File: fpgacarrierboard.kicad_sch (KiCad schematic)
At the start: 0 parts

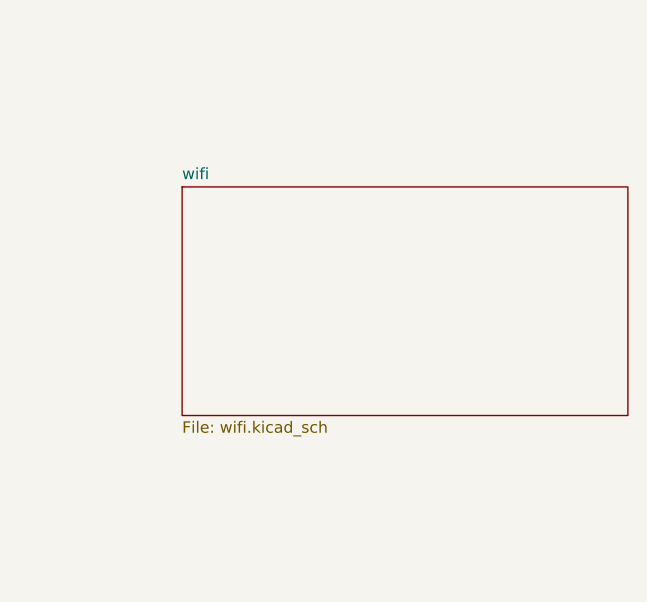
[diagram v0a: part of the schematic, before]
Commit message: Remove optional WiFi sheet from schematic and PCB
- Delete wifi sheet and its seven parts; restore no-connect flags on the five freed FPGA bank-34 pins
- Reduce J4 pad solder-mask margin so the fine-pitch pads meet the 0.1mm web rule
- Regenerate BOM and ERC report
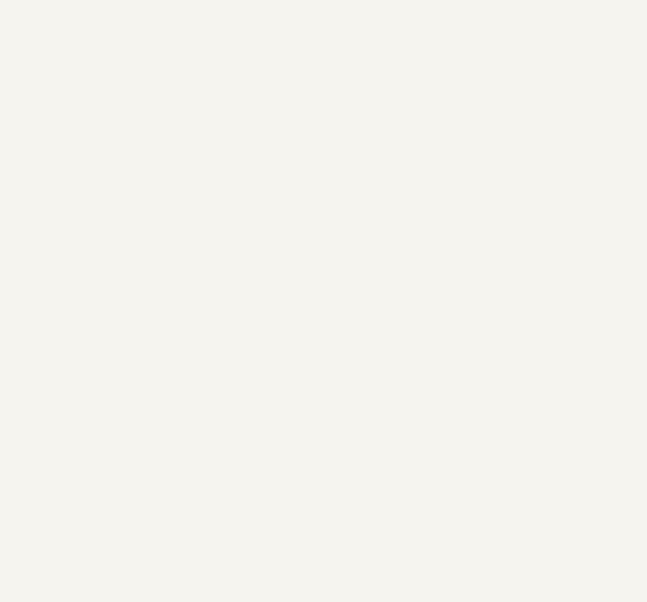
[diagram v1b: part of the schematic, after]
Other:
- removed sheet wifi
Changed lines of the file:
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@@
-	)
-	(sheet
-		(at 186.69 69.85)
-		(size 49.53 25.4)
-		(exclude_from_sim no)
-		(in_bom yes)
-		(on_board yes)
-		(dnp no)
-		(fields_autoplaced yes)
-		(stroke
-			(width 0.1524)
-			(type solid)
-		)
-		(fill
-			(color 0 0 0 0)
-		)
-		(property "Sheetname" "wifi"
-			(at 186.69 69.1384 0)
-			(show_name no)
-			(do_not_autoplace no)
-			(effects
-				(font
-					(size 1.27 1.27)
-				)
-				(justify left bottom)
-			)
-		)
-		(property "Sheetfile" "wifi.kicad_sch"
-			(at 186.69 95.8346 0)
-			(show_name no)
-			(do_not_autoplace no)
-			(effects
-				(font
-					(size 1.27 1.27)
-				)
-				(justify left top)
-			)
-		)
-		(instances
-			(project "fpgacarrierboard"
-				(path "/6b01a127-cba5-44fa-aab9-96b6fa67b92e"
-					(page "11")
-				)
-			)
-		)
 	)
 	(sheet

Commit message: Add optional ESP32-C3 WiFi sheet, convert hand-solder parts to through-hole
- New wifi sheet: ESP32-C3-MINI-1 module on SPI to spare FPGA bank 34, with EN/boot-strap networks, 3V3 bypass/bulk caps and a UART debug header
- Replace SMD hand-solder resistors, LEDs, zener, fuse and ceramic caps with THT equivalents; bulk 10uF/22uF caps become polarized electrolytics
- Fill in LCSC part numbers for the new parts and regenerate BOM and ERC report
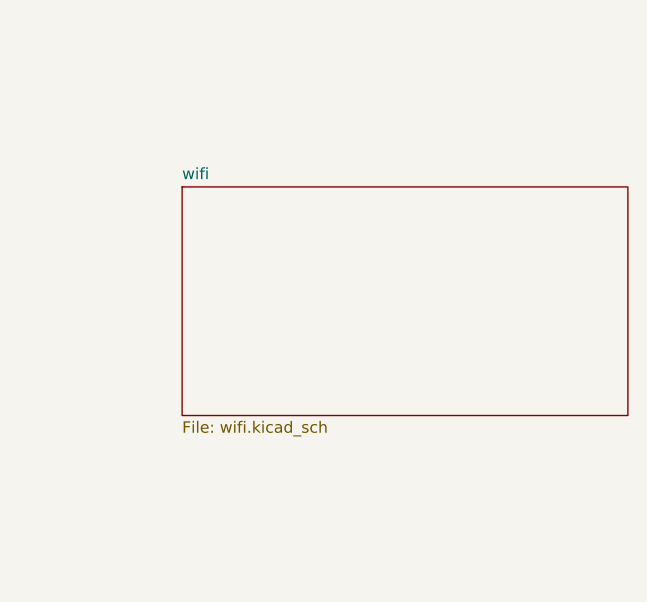
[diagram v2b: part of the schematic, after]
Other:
- added sheet wifi (wifi.kicad_sch)
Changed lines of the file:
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@@
+	)
+	(sheet
+		(at 186.69 69.85)
+		(size 49.53 25.4)
+		(exclude_from_sim no)
+		(in_bom yes)
+		(on_board yes)
+		(dnp no)
+		(fields_autoplaced yes)
+		(stroke
+			(width 0.1524)
+			(type solid)
+		)
+		(fill
+			(color 0 0 0 0)
+		)
+		(property "Sheetname" "wifi"
+			(at 186.69 69.1384 0)
+			(show_name no)
+			(do_not_autoplace no)
+			(effects
+				(font
+					(size 1.27 1.27)
+				)
+				(justify left bottom)
+			)
+		)
+		(property "Sheetfile" "wifi.kicad_sch"
+			(at 186.69 95.8346 0)
+			(show_name no)
+			(do_not_autoplace no)
+			(effects
+				(font
+					(size 1.27 1.27)
+				)
+				(justify left top)
+			)
+		)
+		(instances
+			(project "fpgacarrierboard"
+				(path "/6b01a127-cba5-44fa-aab9-96b6fa67b92e"
+					(page "11")
+				)
+			)
+		)
 	)
 	(sheet
